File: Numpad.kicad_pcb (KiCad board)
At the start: 2 copper layers, 35 parts, among them SW1 SW_PUSH, SW10 SW_PUSH, SW11 SW_PUSH, SW12 SW_PUSH, SW13 SW_PUSH, SW14 SW_PUSH, SW15 SW_PUSH, SW16 SW_PUSH, SW17 SW_PUSH, SW2 SW_PUSH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

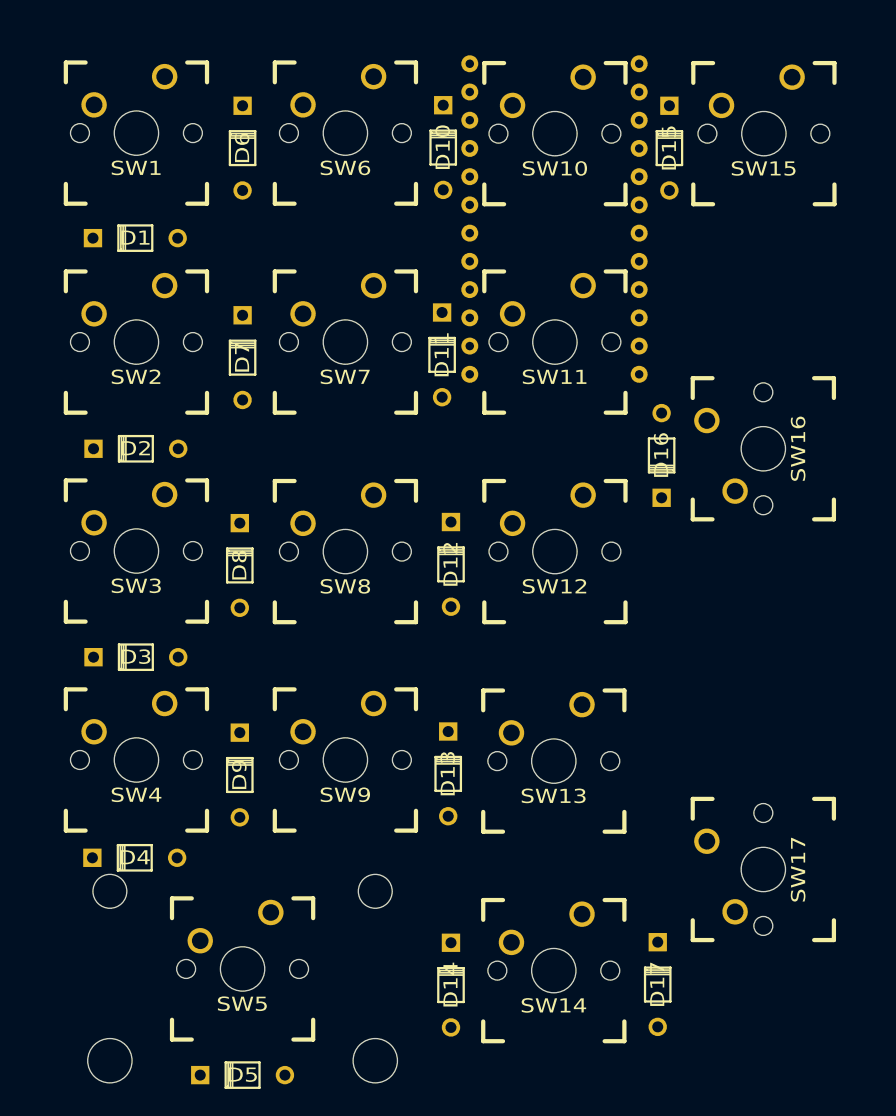
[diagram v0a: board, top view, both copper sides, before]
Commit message: rotated diodes in the schematic. put the switches in the right places
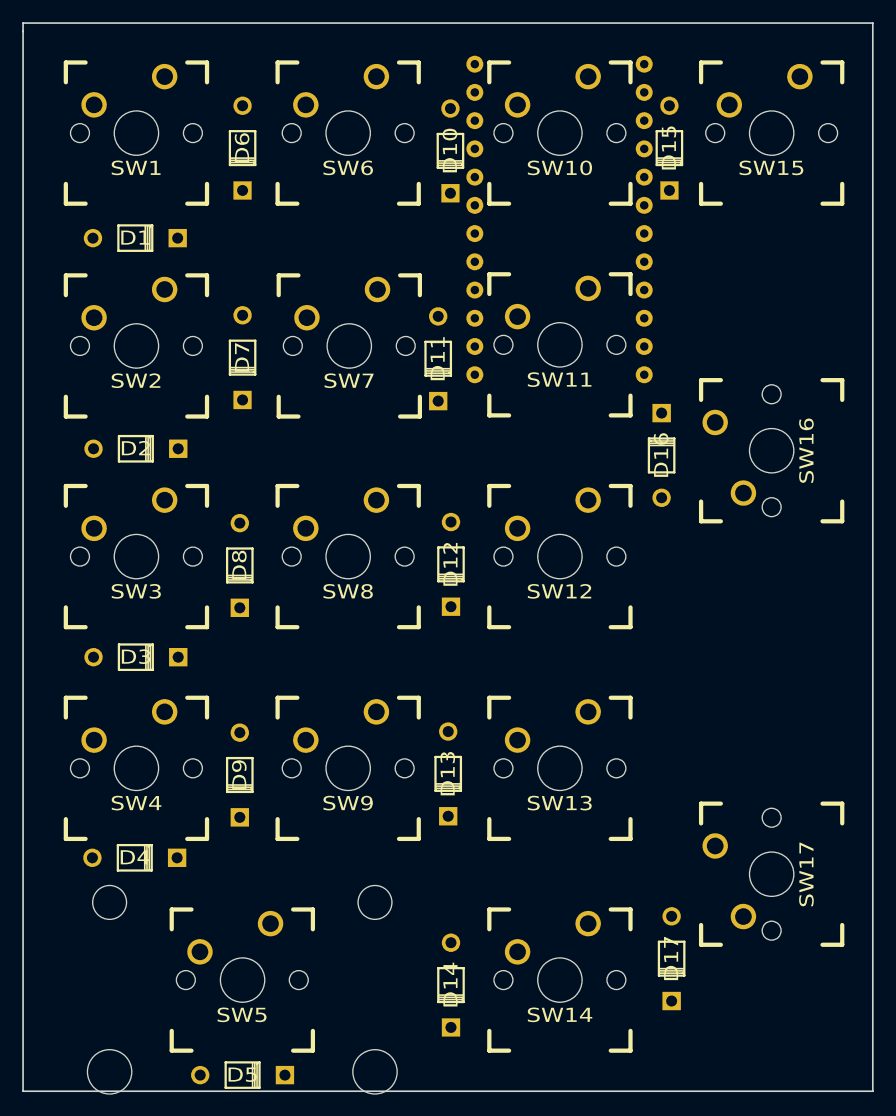
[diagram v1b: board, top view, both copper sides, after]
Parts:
- moved U1 45.6 mm to (92.3, 35.6), turned to 180 degrees
- moved D17 2.64 mm to (92.2, 122.4), turned to 270 degrees
- moved SW14 1.01 mm to (82.2, 124.3)
- moved SW5 1.00 mm to (53.6, 124.3)
- moved SW17 0.86 mm to (101.2, 114.8)
- moved SW13 0.85 mm to (82.2, 105.3)
- moved SW9 0.79 mm to (63.1, 105.3)
- moved SW16 0.77 mm to (101.2, 76.7)
- moved SW4 0.75 mm to (44.0, 105.3)
- moved D10 0.72 mm to (72.3, 49.8), turned to 270 degrees
- moved SW15 0.70 mm to (101.2, 48.1)
- moved SW12 0.64 mm to (82.2, 86.2)
- moved SW11 0.51 mm to (82.2, 67.2)
- moved SW8 0.51 mm to (63.1, 86.2)
- moved SW3 0.50 mm to (44.0, 86.2)
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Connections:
- D10 pad 1: Net-(D1-Pad1) -> Net-(D10-Pad1)
- D10 pad 2: Net-(D10-Pad2) -> Net-(D1-Pad2)
- D15 pad 1: Net-(D1-Pad1) -> Net-(D15-Pad1)
- D15 pad 2: Net-(D15-Pad2) -> Net-(D1-Pad2)
- D16 pad 1: Net-(D11-Pad1) -> Net-(D16-Pad1)
- D16 pad 2: Net-(D16-Pad2) -> Net-(D11-Pad2)
- D17 pad 1: Net-(D14-Pad1) -> Net-(D17-Pad1)
- D17 pad 2: Net-(D17-Pad2) -> Net-(D14-Pad2)
- D2 pad 1: Net-(D11-Pad1) -> Net-(D2-Pad1)
- D2 pad 2: Net-(D2-Pad2) -> Net-(D11-Pad2)
- D3 pad 1: Net-(D12-Pad1) -> Net-(D3-Pad1)
- D3 pad 2: Net-(D3-Pad2) -> Net-(D12-Pad2)
- D4 pad 1: Net-(D13-Pad1) -> Net-(D4-Pad1)
- D4 pad 2: Net-(D4-Pad2) -> Net-(D13-Pad2)
- D5 pad 1: Net-(D14-Pad1) -> Net-(D5-Pad1)
- D5 pad 2: Net-(D5-Pad2) -> Net-(D14-Pad2)
- D6 pad 1: Net-(D1-Pad1) -> Net-(D6-Pad1)
- D6 pad 2: Net-(D6-Pad2) -> Net-(D1-Pad2)
- D7 pad 1: Net-(D11-Pad1) -> Net-(D7-Pad1)
- D7 pad 2: Net-(D7-Pad2) -> Net-(D11-Pad2)
- D8 pad 1: Net-(D12-Pad1) -> Net-(D8-Pad1)
- D8 pad 2: Net-(D8-Pad2) -> Net-(D12-Pad2)
- D9 pad 1: Net-(D13-Pad1) -> Net-(D9-Pad1)
- D9 pad 2: Net-(D9-Pad2) -> Net-(D13-Pad2)
- SW1 pad 2: Net-(D1-Pad2) -> Net-(D1-Pad1)
- SW10 pad 2: Net-(D10-Pad2) -> Net-(D10-Pad1)
- SW11 pad 2: Net-(D11-Pad2) -> Net-(D11-Pad1)
- SW12 pad 2: Net-(D12-Pad2) -> Net-(D12-Pad1)
- SW13 pad 2: Net-(D13-Pad2) -> Net-(D13-Pad1)
- SW14 pad 2: Net-(D14-Pad2) -> Net-(D14-Pad1)
- SW15 pad 2: Net-(D15-Pad2) -> Net-(D15-Pad1)
- SW16 pad 2: Net-(D16-Pad2) -> Net-(D16-Pad1)
- SW17 pad 2: Net-(D17-Pad2) -> Net-(D17-Pad1)
- SW2 pad 2: Net-(D2-Pad2) -> Net-(D2-Pad1)
- SW3 pad 2: Net-(D3-Pad2) -> Net-(D3-Pad1)
- SW4 pad 2: Net-(D4-Pad2) -> Net-(D4-Pad1)
- SW5 pad 2: Net-(D5-Pad2) -> Net-(D5-Pad1)
- SW6 pad 2: Net-(D6-Pad2) -> Net-(D6-Pad1)
- SW7 pad 2: Net-(D7-Pad2) -> Net-(D7-Pad1)
- SW8 pad 2: Net-(D8-Pad2) -> Net-(D8-Pad1)
- SW9 pad 2: Net-(D9-Pad2) -> Net-(D9-Pad1)
- U1 pad 10: Net-(D12-Pad1) -> Net-(D12-Pad2)
- U1 pad 15: Net-(D11-Pad1) -> Net-(D11-Pad2)
- U1 pad 16: Net-(D1-Pad1) -> Net-(D1-Pad2)
- U1 pad 8: Net-(D14-Pad1) -> Net-(D14-Pad2)
- U1 pad 9: Net-(D13-Pad1) -> Net-(D13-Pad2)
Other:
- board outline added: 76.4 x 96.1 mm
